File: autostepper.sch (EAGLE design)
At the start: 22 parts, among them U1 V_REG_317SMD, Y2 SFE_COM-00094

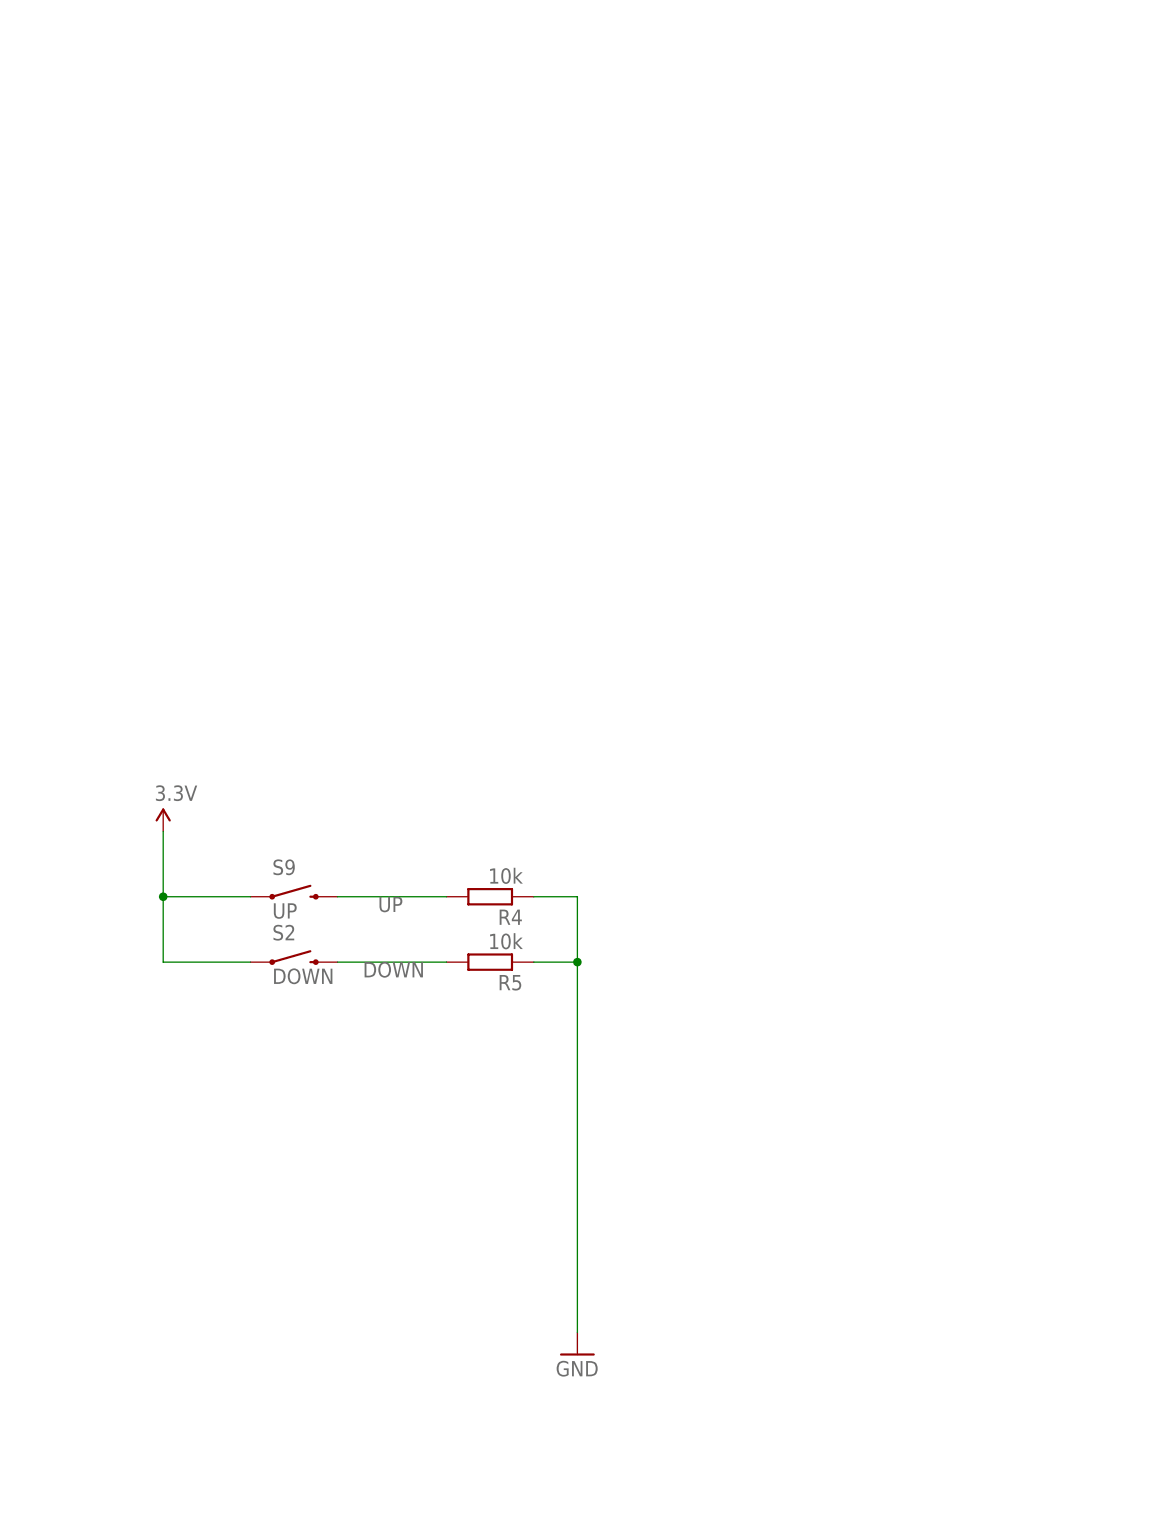
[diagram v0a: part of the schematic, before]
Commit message: Connectors added
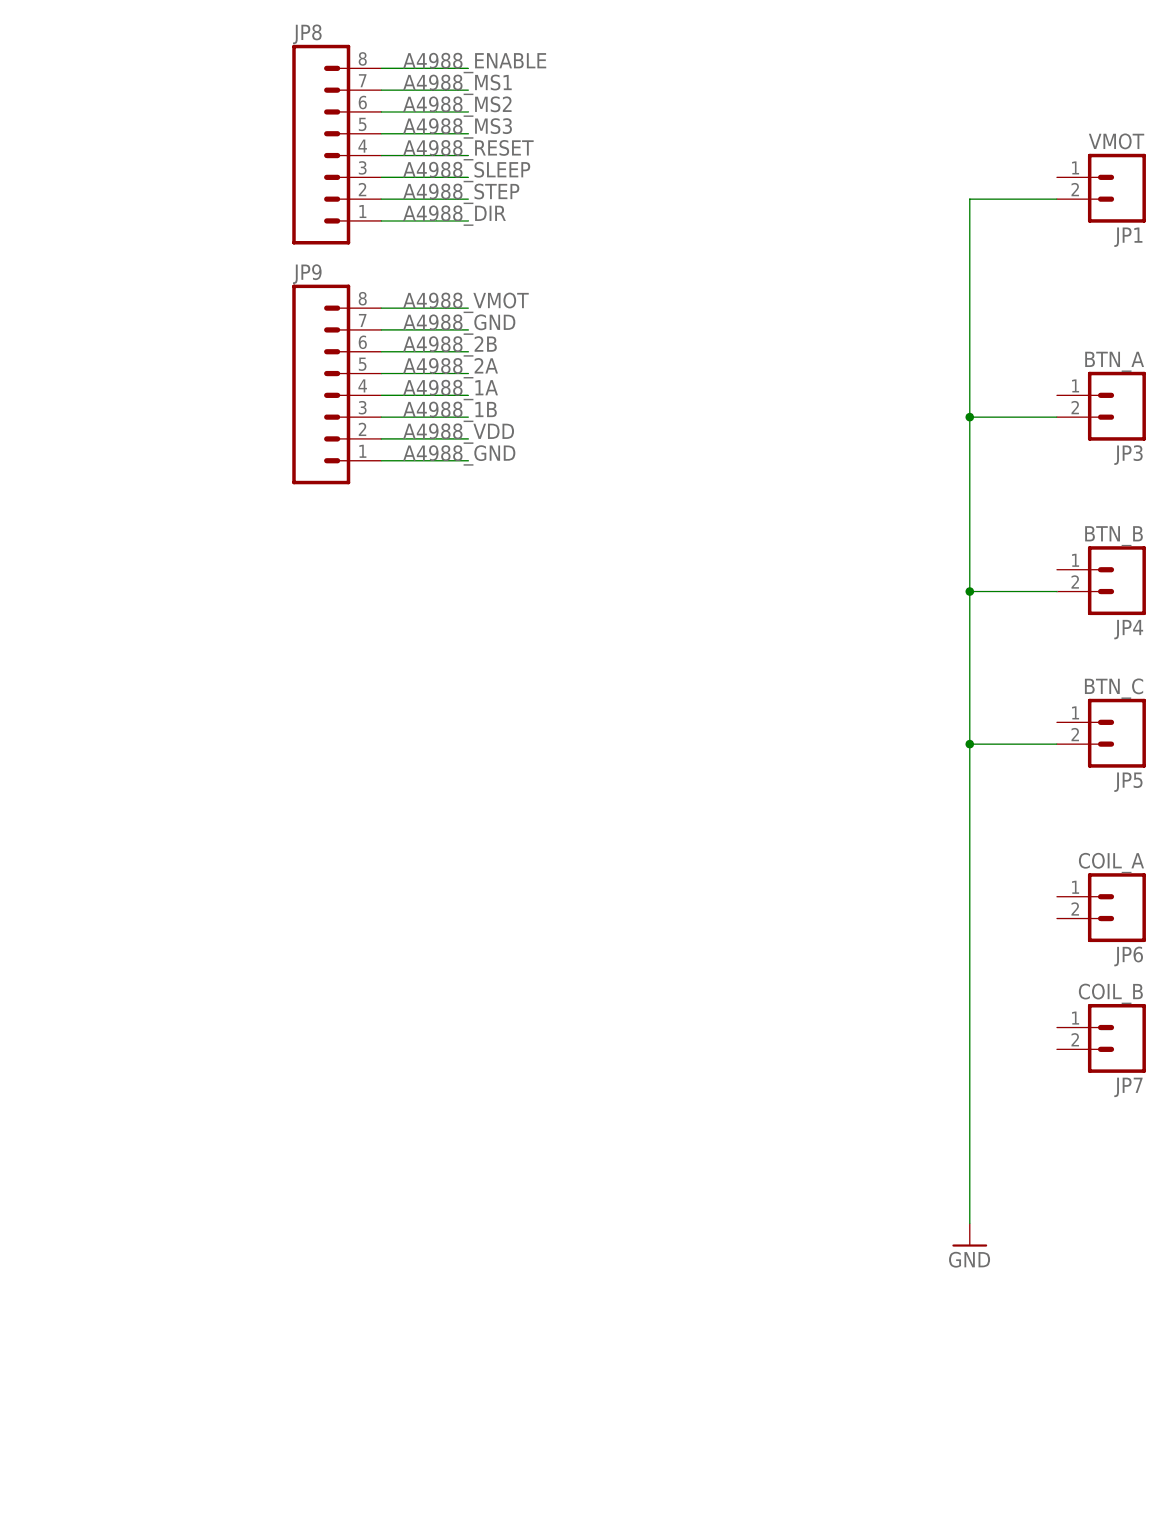
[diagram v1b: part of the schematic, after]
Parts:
- removed R4, R5: 10k, rcl:R-EU_M0805
- removed S2: DOWN, SparkFun-Electromechanical:SWITCH-MOMENTARY-2SMD-4
- removed S9: UP, SparkFun-Electromechanical:SWITCH-MOMENTARY-2SMD-4
- added JP1: VMOT, SparkFun-Connectors:M025MM
- added JP3: BTN_A, SparkFun-Connectors:M025MM
- added JP4: BTN_B, SparkFun-Connectors:M025MM
- added JP5: BTN_C, SparkFun-Connectors:M025MM
- added JP6: COIL_A, SparkFun-Connectors:M025MM
- added JP7: COIL_B, SparkFun-Connectors:M025MM
- added JP8, JP9: (no value), SparkFun-Connectors:M08SMD-COMBO
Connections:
- removed net DOWN: R5.2, S2.2
- removed net UP: R4.2, S9.2
- new net A4988_1A: JP9.4
- new net A4988_1B: JP9.3
- new net A4988_2A: JP9.5
- new net A4988_2B: JP9.6
- new net A4988_DIR: JP8.1
- new net A4988_ENABLE: JP8.8
- new net A4988_GND: JP9.1, JP9.7
- new net A4988_MS1: JP8.7
- new net A4988_MS2: JP8.6
- new net A4988_MS3: JP8.5
- new net A4988_RESET: JP8.4
- new net A4988_SLEEP: JP8.3
- new net A4988_STEP: JP8.2
- new net A4988_VDD: JP9.2
- new net A4988_VMOT: JP9.8
- net 3.3V: no longer S2.1, S9.1
- net GND: now also JP1.2, JP3.2, JP4.2, JP5.2; no longer R4.1, R5.1

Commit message: Layout fix
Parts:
- removed JP3: BTN_A, SparkFun-Connectors:M025MM
- removed JP4: BTN_B, SparkFun-Connectors:M025MM
- removed JP5: BTN_C, SparkFun-Connectors:M025MM
- added C4: 47uF, SparkFun-Passives:CAP_POLD
- added C5: 1uF, SparkFun-Passives:CAP1206
- added C6: .1uF, SparkFun-Passives:CAP1206
- added D1: B340A-13-F, SparkFun-DiscreteSemi:DIODEHV
- added J1: (no value), SparkFun-Connectors:M04LONGPADS
- JP8, JP9: device SparkFun-Connectors:M08SMD-COMBO -> SparkFun-Connectors:M08LONGPADS
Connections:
- removed net N$3: R6.2, U1.OUT
- new net BUTTON_A: J1.1, U$1.PD4(ADC8)
- new net BUTTON_B: J1.2, U$1.PC6
- new net BUTTON_C: J1.3, U$1.PD7(ADC10)
- new net N$8: C4.+, C6.1, D1.C, U1.IN
- net 3.3V: now also C5.1, R14.1, R6.2, U1.OUT
- net A4988_1A: now also JP6.2, JP7.1
- net A4988_1B: now also JP7.2
- net A4988_2A: now also JP6.1
- net A4988_VMOT: now also D1.A, JP1.1
- net GND: now also C4.-, C5.2, C6.2, J1.4; no longer JP3.2, JP4.2, JP5.2
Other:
- moved on the sheet: JP6, JP7, LED3, R14
